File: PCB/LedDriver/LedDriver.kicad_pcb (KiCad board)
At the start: 2 copper layers, 101.6 x 101.6 mm, 157 parts, among them J101 LCD, J102 TweLite-R, J103 Conn_01x02_Male, J104 Conn_01x08_Male, J105 Conn_01x08_Male, J106 Conn_01x08_Male, J107 Conn_01x02_Male, J108 Barrel_Jack_Switch, J109 Conn_01x02_Male, J110 Conn_01x02_Male, SW101 SW_Push, SW102 SW_Push, SW103 SW_Push, SW104 SW_Push, SW105 SW_Push, SW106 SW_Push, SW107 SW_Push, U101 MW-R-WX, U201 NJW4617DL3-TE1, U202 NJW4617DL3-TE1, U203 NJW4617DL3-TE1, U204 NJW4617DL3-TE1, U205 NJW4617DL3-TE1, U206 NJW4617DL3-TE1, U207 NJW4617DL3-TE1, U208 74HC595, U301 NJW4617DL3-TE1, U302 NJW4617DL3-TE1, U303 NJW4617DL3-TE1, U304 NJW4617DL3-TE1, U305 NJW4617DL3-TE1, U306 NJW4617DL3-TE1, U307 NJW4617DL3-TE1, U308 74HC595, U401 NJW4617DL3-TE1, U402 NJW4617DL3-TE1, U403 NJW4617DL3-TE1, U404 NJW4617DL3-TE1, U405 NJW4617DL3-TE1, U406 NJW4617DL3-TE1, U407 NJW4617DL3-TE1, U408 74HC595

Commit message: 基板改良
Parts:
- added C106: 10u, Capacitor_SMD:C_0603_1608Metric, B.Cu at (240.0, 154.9)
- added C107: 10u, Capacitor_SMD:C_0603_1608Metric, B.Cu at (240.0, 142.2)
- added C108: 10u, Capacitor_SMD:C_0603_1608Metric, B.Cu at (219.7, 158.8)
- added C201: 0.1u, Capacitor_SMD:C_0603_1608Metric, B.Cu at (161.3, 49.5)
- added C202: 0.1u, Capacitor_SMD:C_0603_1608Metric, B.Cu at (161.3, 64.8)
- added C203: 0.1u, Capacitor_SMD:C_0603_1608Metric, B.Cu at (161.3, 80.0)
- added C204: 0.1u, Capacitor_SMD:C_0603_1608Metric, B.Cu at (161.3, 95.2)
- added C205: 0.1u, Capacitor_SMD:C_0603_1608Metric, B.Cu at (161.3, 110.5)
- added C206: 0.1u, Capacitor_SMD:C_0603_1608Metric, B.Cu at (161.3, 125.7)
- added C207: 0.1u, Capacitor_SMD:C_0603_1608Metric, B.Cu at (161.3, 141.0)
- added C208: 0.1u, Capacitor_SMD:C_0603_1608Metric, B.Cu at (143.5, 154.9)
- added C301: 0.1u, Capacitor_SMD:C_0603_1608Metric, B.Cu at (191.8, 49.5)
- added C302: 0.1u, Capacitor_SMD:C_0603_1608Metric, B.Cu at (191.8, 64.8)
- added C303: 0.1u, Capacitor_SMD:C_0603_1608Metric, B.Cu at (191.8, 80.0)
- added C304: 0.1u, Capacitor_SMD:C_0603_1608Metric, B.Cu at (191.8, 95.2)
- added C305: 0.1u, Capacitor_SMD:C_0603_1608Metric, B.Cu at (191.8, 110.5)
- added C306: 0.1u, Capacitor_SMD:C_0603_1608Metric, B.Cu at (191.8, 125.7)
- added C307: 0.1u, Capacitor_SMD:C_0603_1608Metric, B.Cu at (191.8, 141.0)
- added C308: 0.1u, Capacitor_SMD:C_0603_1608Metric, B.Cu at (174.0, 154.9)
- added C401: 0.1u, Capacitor_SMD:C_0603_1608Metric, B.Cu at (222.2, 49.5)
- added C402: 0.1u, Capacitor_SMD:C_0603_1608Metric, B.Cu at (222.2, 64.8)
- added C403: 0.1u, Capacitor_SMD:C_0603_1608Metric, B.Cu at (222.2, 80.0)
- added C404: 0.1u, Capacitor_SMD:C_0603_1608Metric, B.Cu at (222.2, 95.2)
- added C405: 0.1u, Capacitor_SMD:C_0603_1608Metric, B.Cu at (222.2, 110.5)
- added C406: 0.1u, Capacitor_SMD:C_0603_1608Metric, B.Cu at (222.2, 125.7)
- added C407: 0.1u, Capacitor_SMD:C_0603_1608Metric, B.Cu at (222.2, 141.0)
- added C408: 0.1u, Capacitor_SMD:C_0603_1608Metric, B.Cu at (204.5, 154.9)
- added H105: MountingHole, MountingHole:MountingHole_6.4mm_M6, F.Cu at (128.3, 52.1)
- added J111: Conn_01x02_Male, Connector_JST:JST_XH_B2B-XH-A_1x02_P2.50mm_Vertical, B.Cu at (214.6, 158.8)
- added U102: LM1117-3.3, Package_TO_SOT_SMD:SOT-223-3_TabPin2, B.Cu at (240.0, 148.6)
- C102: value 0.1u -> 10u; footprint Capacitor_SMD:C_1206_3216Metric -> Capacitor_SMD:C_0603_1608Metric
- C103: value 10u -> 0.1u; footprint Capacitor_THT:CP_Radial_D10.0mm_P5.00mm -> Capacitor_SMD:C_0603_1608Metric
- C104: footprint Capacitor_SMD:C_0603_1608Metric -> Capacitor_SMD:C_1206_3216Metric
- C105: value 47u -> 10u; footprint Capacitor_SMD:C_0603_1608Metric -> Capacitor_THT:CP_Radial_D10.0mm_P5.00mm; moved to F.Cu
- J102: value TweLite-R -> Conn_01x07_Female; footprint Connector_PinSocket_2.54mm:PinSocket_1x06_P2.54mm_Vertical -> Connector_PinSocket_2.54mm:PinSocket_1x07_P2.54mm_Vertical
- J104: value Conn_01x08_Male -> Conn_01x02_Male; footprint Connector_JST:JST_VH_B8P-VH_1x08_P3.96mm_Vertical -> Connector_JST:JST_VH_B2P-VH_1x02_P3.96mm_Vertical
- J105, J106: value Conn_01x08_Male -> Conn_01x02_Male; footprint Connector_JST:JST_VH_B8P-VH_1x08_P3.96mm_Vertical -> Connector_PinHeader_2.54mm:PinHeader_1x02_P2.54mm_Vertical
- J107: value Conn_01x02_Male -> DC+5V; footprint Connector_JST:JST_VH_B2P-VH_1x02_P3.96mm_Vertical -> Connector_BarrelJack:BarrelJack_CUI_PJ-102AH_Horizontal
- J108: value Barrel_Jack_Switch -> Conn_01x08_Male; footprint Connector_BarrelJack:BarrelJack_CUI_PJ-102AH_Horizontal -> Connector_JST:JST_VH_B8P-VH_1x08_P3.96mm_Vertical
- J109, J110: value Conn_01x02_Male -> Conn_01x08_Male; footprint Connector_PinHeader_2.54mm:PinHeader_1x02_P2.54mm_Vertical -> Connector_JST:JST_VH_B8P-VH_1x08_P3.96mm_Vertical
- R201, R204, R207, R210, R213, R216, R219, R301, R304, R307, R310, R313, R316, R319, R401, R404, R407, R410, R413, R416, R419: value 680 -> 1.2k
- R202, R205, R208, R211, R214, R217, R220, R302, R305, R308, R311, R314, R317, R320, R402, R405, R408, R411, R414, R417, R420: value 0.33 -> 0.20; footprint Resistor_THT:R_Axial_DIN0207_L6.3mm_D2.5mm_P7.62mm_Horizontal -> Resistor_THT:R_Axial_DIN0207_L6.3mm_D2.5mm_P10.16mm_Horizontal; moved to F.Cu
- R203, R206, R209, R212, R215, R218, R221, R303, R306, R309, R312, R315, R318, R321, R403, R406, R409, R412, R415, R418, R421: value 0.33 -> 0.47; footprint Resistor_THT:R_Axial_DIN0207_L6.3mm_D2.5mm_P7.62mm_Horizontal -> Resistor_THT:R_Axial_DIN0207_L6.3mm_D2.5mm_P10.16mm_Horizontal; moved to F.Cu
- R222, R223, R224, R225, R226, R227, R228, R322, R323, R324, R325, R326, R327, R328, R422, R423, R424, R425, R426, R427, R428: value 1k -> 1.2k
- U201, U202, U203, U204, U205, U206, U207: moved to B.Cu
- moved J110 152.3 mm to (238.8, 47.6), turned to -90 degrees
- moved J107 131.0 mm to (232.9, 155.1)
- moved R322 126.3 mm to (188.0, 52.1), turned to 90 degrees
- moved J109 123.1 mm to (208.3, 47.6), turned to -90 degrees
- moved R328 116.8 mm to (188.0, 143.5), turned to 90 degrees
- moved R302 114.4 mm to (198.1, 55.9), turned to 180 degrees
- moved R305 114.4 mm to (198.1, 71.1), turned to 180 degrees
- moved R308 114.3 mm to (198.1, 86.4), turned to 180 degrees
- moved R311 114.3 mm to (198.1, 101.6), turned to 180 degrees
- moved R320 114.3 mm to (198.1, 147.3), turned to 180 degrees
- moved R314 114.3 mm to (198.1, 116.8), turned to 180 degrees
- moved R317 114.3 mm to (198.1, 132.1), turned to 180 degrees
- moved R422 114.1 mm to (218.4, 52.1), turned to 90 degrees
- moved J108 113.4 mm to (177.8, 47.6), turned to -90 degrees
- moved D301 108.7 mm to (195.6, 52.1)
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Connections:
- C102 pad 1: VDD -> GND
- C102 pad 2: GND -> +3.3V
- C103 pad 1: VDD -> +3.3V
- C104 pad 1: +3.3V -> VDD
- C105 pad 1: +3.3V -> VDD
- J104 pad 2: /digitDriver_one/A -> GND
- J105 pad 1: VDD -> /add_01
- J105 pad 2: /digitDriver_ten/A -> GND
- J106 pad 1: VDD -> /add_02
- J106 pad 2: /digitDriver_hun/A -> GND
- J107 pad 1: VDD -> Net-(C106-Pad1)
- J108 pad 1: +3.3V -> VDD
- J108 pad 2: GND -> /digitDriver_one/A
- J108 pad 3: unconnected-(J108-Pad3) -> /digitDriver_one/B
- J109 pad 1: /add_01 -> VDD
- J109 pad 2: GND -> /digitDriver_ten/A
- J110 pad 1: /add_02 -> VDD
- J110 pad 2: GND -> /digitDriver_hun/A
- R203 pad 1: Net-(R202-Pad1) -> Net-(R202-Pad2)
- R206 pad 1: Net-(R205-Pad1) -> Net-(R205-Pad2)
- R209 pad 1: Net-(R208-Pad1) -> Net-(R208-Pad2)
- R212 pad 1: Net-(R211-Pad1) -> Net-(R211-Pad2)
- R215 pad 1: Net-(R214-Pad1) -> Net-(R214-Pad2)
- R218 pad 1: Net-(R217-Pad1) -> Net-(R217-Pad2)
- R221 pad 1: Net-(R220-Pad1) -> Net-(R220-Pad2)
- R222 pad 1: /digitDriver_one/QG -> /digitDriver_one/QA
- R223 pad 1: /digitDriver_one/QF -> /digitDriver_one/QB
- R224 pad 1: /digitDriver_one/QE -> /digitDriver_one/QC
- R226 pad 1: /digitDriver_one/QC -> /digitDriver_one/QE
- R227 pad 1: /digitDriver_one/QB -> /digitDriver_one/QF
- R228 pad 1: /digitDriver_one/QA -> /digitDriver_one/QG
- R303 pad 1: Net-(R302-Pad1) -> Net-(R302-Pad2)
- R306 pad 1: Net-(R305-Pad1) -> Net-(R305-Pad2)
- R309 pad 1: Net-(R308-Pad1) -> Net-(R308-Pad2)
- R312 pad 1: Net-(R311-Pad1) -> Net-(R311-Pad2)
- R315 pad 1: Net-(R314-Pad1) -> Net-(R314-Pad2)
- R318 pad 1: Net-(R317-Pad1) -> Net-(R317-Pad2)
- R321 pad 1: Net-(R320-Pad1) -> Net-(R320-Pad2)
- R322 pad 1: /digitDriver_ten/QG -> /digitDriver_ten/QA
- R323 pad 1: /digitDriver_ten/QF -> /digitDriver_ten/QB
- R324 pad 1: /digitDriver_ten/QE -> /digitDriver_ten/QC
- R326 pad 1: /digitDriver_ten/QC -> /digitDriver_ten/QE
- R327 pad 1: /digitDriver_ten/QB -> /digitDriver_ten/QF
- R328 pad 1: /digitDriver_ten/QA -> /digitDriver_ten/QG
- R403 pad 1: Net-(R402-Pad1) -> Net-(R402-Pad2)
- R406 pad 1: Net-(R405-Pad1) -> Net-(R405-Pad2)
- R409 pad 1: Net-(R408-Pad1) -> Net-(R408-Pad2)
- R412 pad 1: Net-(R411-Pad1) -> Net-(R411-Pad2)
- R415 pad 1: Net-(R414-Pad1) -> Net-(R414-Pad2)
- R418 pad 1: Net-(R417-Pad1) -> Net-(R417-Pad2)
- R421 pad 1: Net-(R420-Pad1) -> Net-(R420-Pad2)
- R422 pad 1: /digitDriver_hun/QG -> /digitDriver_hun/QA
- R423 pad 1: /digitDriver_hun/QF -> /digitDriver_hun/QB
- R424 pad 1: /digitDriver_hun/QE -> /digitDriver_hun/QC
- R426 pad 1: /digitDriver_hun/QC -> /digitDriver_hun/QE
- R427 pad 1: /digitDriver_hun/QB -> /digitDriver_hun/QF
- R428 pad 1: /digitDriver_hun/QA -> /digitDriver_hun/QG
- U201 pad 4: Net-(R202-Pad2) -> Net-(R202-Pad1)
- U202 pad 4: Net-(R205-Pad2) -> Net-(R205-Pad1)
- U203 pad 4: Net-(R208-Pad2) -> Net-(R208-Pad1)
- U204 pad 4: Net-(R211-Pad2) -> Net-(R211-Pad1)
- U205 pad 4: Net-(R214-Pad2) -> Net-(R214-Pad1)
- U206 pad 4: Net-(R217-Pad2) -> Net-(R217-Pad1)
- U207 pad 4: Net-(R220-Pad2) -> Net-(R220-Pad1)
- U301 pad 4: Net-(R302-Pad2) -> Net-(R302-Pad1)
- U302 pad 4: Net-(R305-Pad2) -> Net-(R305-Pad1)
- U303 pad 4: Net-(R308-Pad2) -> Net-(R308-Pad1)
- U304 pad 4: Net-(R311-Pad2) -> Net-(R311-Pad1)
- U305 pad 4: Net-(R314-Pad2) -> Net-(R314-Pad1)
- U306 pad 4: Net-(R317-Pad2) -> Net-(R317-Pad1)
- U307 pad 4: Net-(R320-Pad2) -> Net-(R320-Pad1)
- U401 pad 4: Net-(R402-Pad2) -> Net-(R402-Pad1)
- U402 pad 4: Net-(R405-Pad2) -> Net-(R405-Pad1)
- U403 pad 4: Net-(R408-Pad2) -> Net-(R408-Pad1)
- U404 pad 4: Net-(R411-Pad2) -> Net-(R411-Pad1)
- U405 pad 4: Net-(R414-Pad2) -> Net-(R414-Pad1)
- U406 pad 4: Net-(R417-Pad2) -> Net-(R417-Pad1)
- U407 pad 4: Net-(R420-Pad2) -> Net-(R420-Pad1)
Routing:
- net +3.3V: track 510.8 -> 795.7 mm, vias 10 -> 1
- net /digitDriver_ten/QG: track 78.4 -> 12.4 mm, vias 1 -> 2
- net /digitDriver_ten/F: track 118.3 -> 62.6 mm
- net /digitDriver_hun/QG: track 70.3 -> 15.6 mm, vias 2 -> 1
- net /digitDriver_ten/QF: track 66.0 -> 24.6 mm, vias 2 -> 1
- net /digitDriver_ten/QC: track 33.6 -> 71.9 mm, vias 1 -> 2
- net /SCK: track 89.6 -> 127.2 mm, vias 3 -> 2
- net /digitDriver_ten/QB: track 52.3 -> 88.5 mm, vias 1 -> 2
- net /digitDriver_hun/QC: track 36.4 -> 72.5 mm
- net /RESET: track 97.1 -> 132.6 mm
- net /_G: track 81.1 -> 115.1 mm, vias 3 -> 0
- net Net-(C106-Pad1): track 0.00 -> 33.5 mm
- net /SI: track 36.9 -> 68.7 mm
- net /_SCLR: track 78.2 -> 109.8 mm
- net /SCL: track 31.3 -> 61.8 mm
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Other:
- board size 101.6 x 101.6 mm -> 125.7 x 125.7 mm
- board text removed: "+"
- board text removed: "+ -"
- board text removed: "-"
- board text removed: "1"
- board text removed: "1'"
- board text removed: "10'"
- board text removed: "100'"
- board text removed: "ADDR_H"
- board text removed: "ADDR_L"
- board text removed: "Ah"
- board text removed: "Ao"
- board text removed: "At"
- board text removed: "Bh"
- board text removed: "Bo"
- board text removed: "Bt"
- board text removed: "Ch"
- board text removed: "Co"
- board text removed: "Ct"
- board text removed: "DC3.3V"
- board text removed: "DC36V"
- board text removed: "Dh"
- board text removed: "Do"
- board text removed: "Dt"
- board text removed: "Eh"
- board text removed: "Eo"
- board text removed: "Et"
- board text removed: "Fh"
- board text removed: "Fo"
- board text removed: "Ft"
- board text removed: "Gh"
- board text removed: "Go"
- board text removed: "Gt"
- board text removed: "Reset"

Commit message: 回路修正
三端子レギュレータ追加
GNDパターン修正
currentパターン同士のクリアランスを確保
ファン端子追加
温度センサ追加
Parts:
- added C109: 0.1u, Capacitor_SMD:C_0603_1608Metric, B.Cu at (201.3, 114.9)
- added U103: LM35-LP, Package_TO_SOT_THT:TO-92_Inline_Horizontal1, F.Cu at (203.2, 116.2)
- SW101, SW102, SW103, SW104, SW105, SW106, SW107: footprint Button_Switch_SMD:SW_SPST_B3S-1000 -> Library:SW_SPST_B3S-1000
- moved C107 113.1 mm to (127.0, 146.1)
- moved U102 113.1 mm to (127.0, 152.4)
- moved C106 111.8 mm to (128.3, 158.1)
- moved J107 99.1 mm to (134.0, 149.2)
- moved J111 21.6 mm to (236.2, 159.4)
- moved C108 15.6 mm to (234.9, 155.6), turned to 180 degrees
- moved C102 9.40 mm to (141.7, 119.6)
- moved C101 8.77 mm to (139.8, 119.6)
- moved U101 7.56 mm to (130.9, 119.6)
- moved R101 4.02 mm to (147.3, 152.4)
- moved SW101 4.02 mm to (147.3, 147.3)
- moved SW103 4.02 mm to (147.3, 139.7)
- moved SW105 4.02 mm to (137.2, 139.7)
- moved SW107 4.02 mm to (127.0, 139.7)
- moved SW102 4.02 mm to (147.3, 132.1)
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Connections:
- U101 pad 23: unconnected-(U101-Pad23) -> /ADC1
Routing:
- net VDD: track 37.6 -> 228.0 mm
- net Net-(C106-Pad1): track 33.5 -> 136.9 mm
- net /ADC1: track 0.00 -> 87.0 mm, vias 0 -> 1
- net +3.3V: track 795.7 -> 828.2 mm, vias 1 -> 3
- net /SI: track 68.7 -> 40.5 mm, vias 2 -> 0
- net /PlusHun: track 17.3 -> 3.77 mm
- net /TX: track 39.3 -> 52.6 mm
- net /SCK: track 127.2 -> 114.3 mm, vias 2 -> 3
- net /_SCLR: track 109.8 -> 122.6 mm, vias 3 -> 2
- net /MinusHun: track 24.6 -> 13.1 mm
- net /RCK: track 111.4 -> 120.6 mm, vias 2 -> 0
- net /PRG: track 30.7 -> 24.7 mm
- net Net-(R402-Pad1): track 10.4 -> 5.80 mm, vias 1 -> 0
- net Net-(R202-Pad1): track 10.5 -> 5.97 mm, vias 1 -> 0
- net /PlusOne: track 21.1 -> 17.1 mm
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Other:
- board text added: "+"
- board text added: "-"
- board text added: "1'"
- board text added: "1'A"
- board text added: "1'B"
- board text added: "1'C"
- board text added: "1'D"
- board text added: "1'E"
- board text added: "1'F"
- board text added: "1'G"
- board text added: "10'"
- board text added: "10'A"
- board text added: "10'B"
- board text added: "10'C"
- board text added: "10'D"
- board text added: "10'E"
- board text added: "10'F"
- board text added: "10'G"
- board text added: "100'"
- board text added: "100'A"
- board text added: "100'B"
- board text added: "100'C"
- board text added: "100'D"
- board text added: "100'E"
- board text added: "100'F"
- board text added: "100'G"
- board text added: "Addr1"
- board text added: "Addr2"
- board text added: "DC +5V"
- board text added: "DC 36V"
- board text added: "EXT"
- board text added: "Fan +5V"
- board text added: "LCD"
- board text added: "T-sens"
- board text added: "TWE-R"

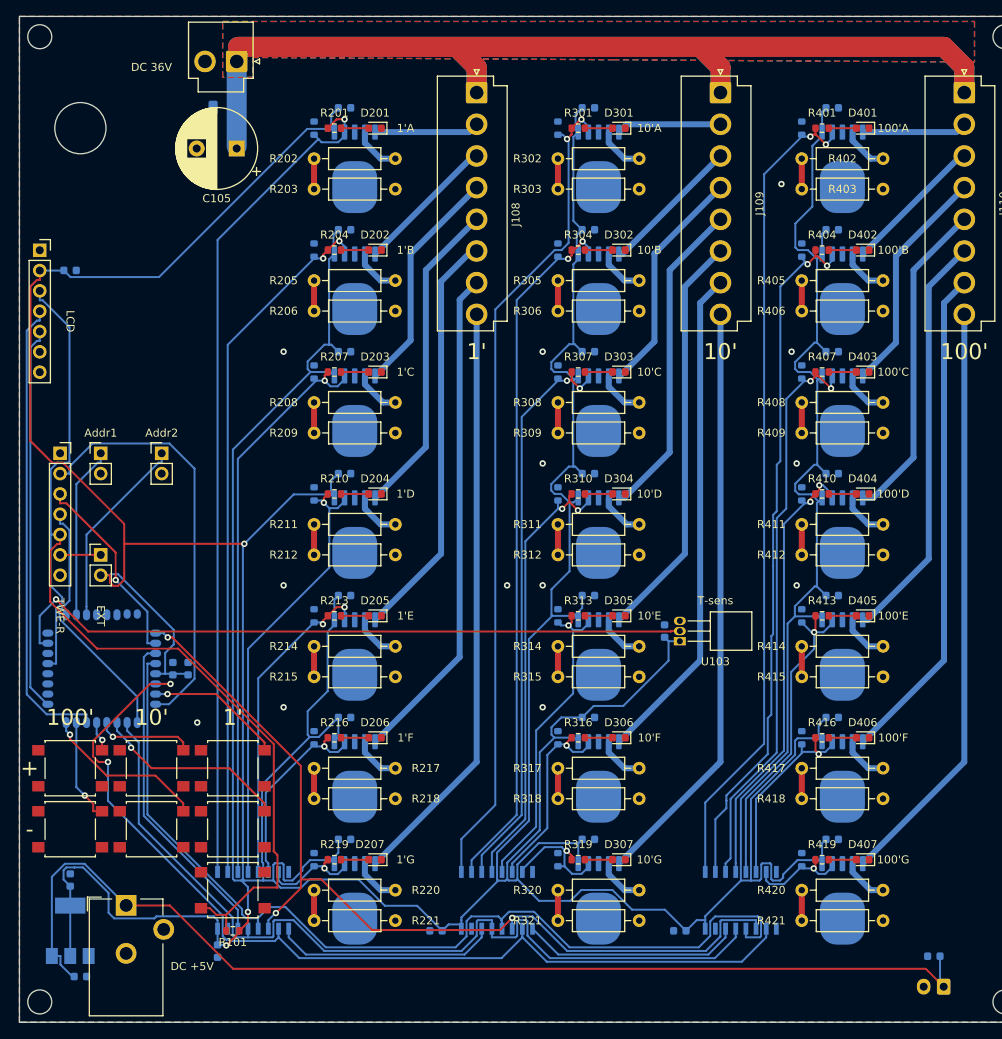
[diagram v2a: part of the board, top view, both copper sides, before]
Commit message: パターン修正
LEDドライバのパスコンを最短で配線
LEDドライバのタブをGNDに配線
平行な信号パターン同士の距離を開け、GNDパターンを間に追加
直角なパターンを修正
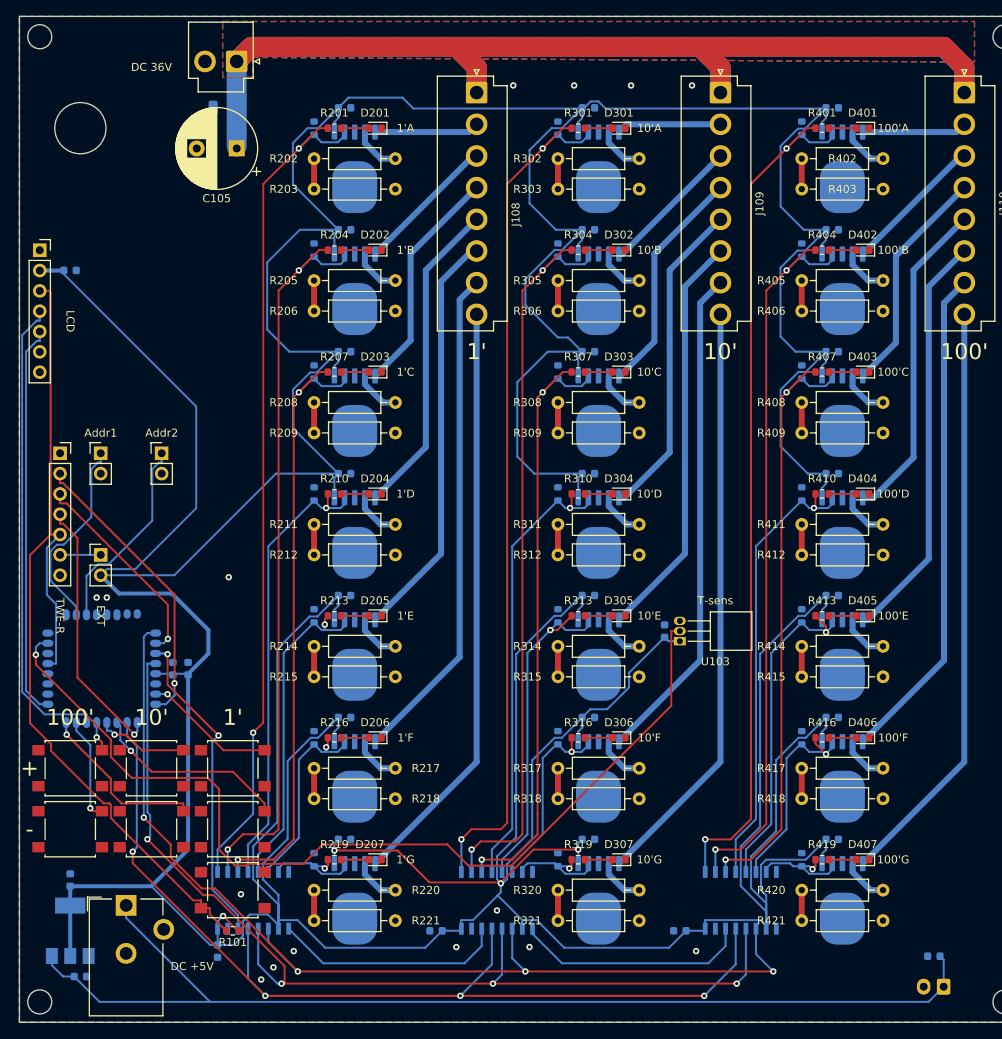
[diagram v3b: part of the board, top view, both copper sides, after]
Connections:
- U101 pad 6: /_SCLR -> unconnected-(U101-Pad6)
- U201 pad 6: unconnected-(U201-Pad6) -> GND
- U202 pad 6: unconnected-(U202-Pad6) -> GND
- U203 pad 6: unconnected-(U203-Pad6) -> GND
- U204 pad 6: unconnected-(U204-Pad6) -> GND
- U205 pad 6: unconnected-(U205-Pad6) -> GND
- U206 pad 6: unconnected-(U206-Pad6) -> GND
- U207 pad 6: unconnected-(U207-Pad6) -> GND
- U208 pad 10: /_SCLR -> +3.3V
- U301 pad 6: unconnected-(U301-Pad6) -> GND
- U302 pad 6: unconnected-(U302-Pad6) -> GND
- U303 pad 6: unconnected-(U303-Pad6) -> GND
- U304 pad 6: unconnected-(U304-Pad6) -> GND
- U305 pad 6: unconnected-(U305-Pad6) -> GND
- U306 pad 6: unconnected-(U306-Pad6) -> GND
- U307 pad 6: unconnected-(U307-Pad6) -> GND
- U308 pad 10: /_SCLR -> +3.3V
- U401 pad 6: unconnected-(U401-Pad6) -> GND
- U402 pad 6: unconnected-(U402-Pad6) -> GND
- U403 pad 6: unconnected-(U403-Pad6) -> GND
- U404 pad 6: unconnected-(U404-Pad6) -> GND
- U405 pad 6: unconnected-(U405-Pad6) -> GND
- U406 pad 6: unconnected-(U406-Pad6) -> GND
- U407 pad 6: unconnected-(U407-Pad6) -> GND
- U408 pad 10: /_SCLR -> +3.3V
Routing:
- net /_SCLR: track 122.6 -> 0.00 mm, vias 2 -> 0
- net +3.3V: track 828.2 -> 903.5 mm, vias 3 -> 4
- net /ADC1: track 87.0 -> 120.3 mm
- net /SCK: track 114.3 -> 131.0 mm, vias 3 -> 4
- net /TX: track 52.6 -> 36.7 mm, vias 0 -> 1
- net /RESET: track 129.1 -> 113.6 mm
- net /_G: track 111.6 -> 125.9 mm, vias 0 -> 4
- net /RCK: track 120.6 -> 129.1 mm, vias 0 -> 4
- net /digitDriver_one/QC: track 71.7 -> 78.2 mm, vias 1 -> 2
- net /digitDriver_ten/QB: track 87.6 -> 93.9 mm
- net /digitDriver_one/QB: track 87.6 -> 93.6 mm
- net /digitDriver_ten/QC: track 71.8 -> 77.6 mm
- net /digitDriver_hun/QA: track 103.5 -> 108.9 mm
- net /digitDriver_hun/QB: track 88.0 -> 93.2 mm
- net /digitDriver_hun/QC: track 72.3 -> 77.2 mm
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
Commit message: パターン修正
シフトレジスタ信号線と平行な3.3Vラインを移動
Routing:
- net +3.3V: track 903.5 -> 788.5 mm, vias 4 -> 13
- net /ADC1: track 120.3 -> 127.8 mm
- net /digitDriver_hun/QF: track 26.5 -> 28.7 mm
- net /digitDriver_hun/QE: track 42.2 -> 43.7 mm

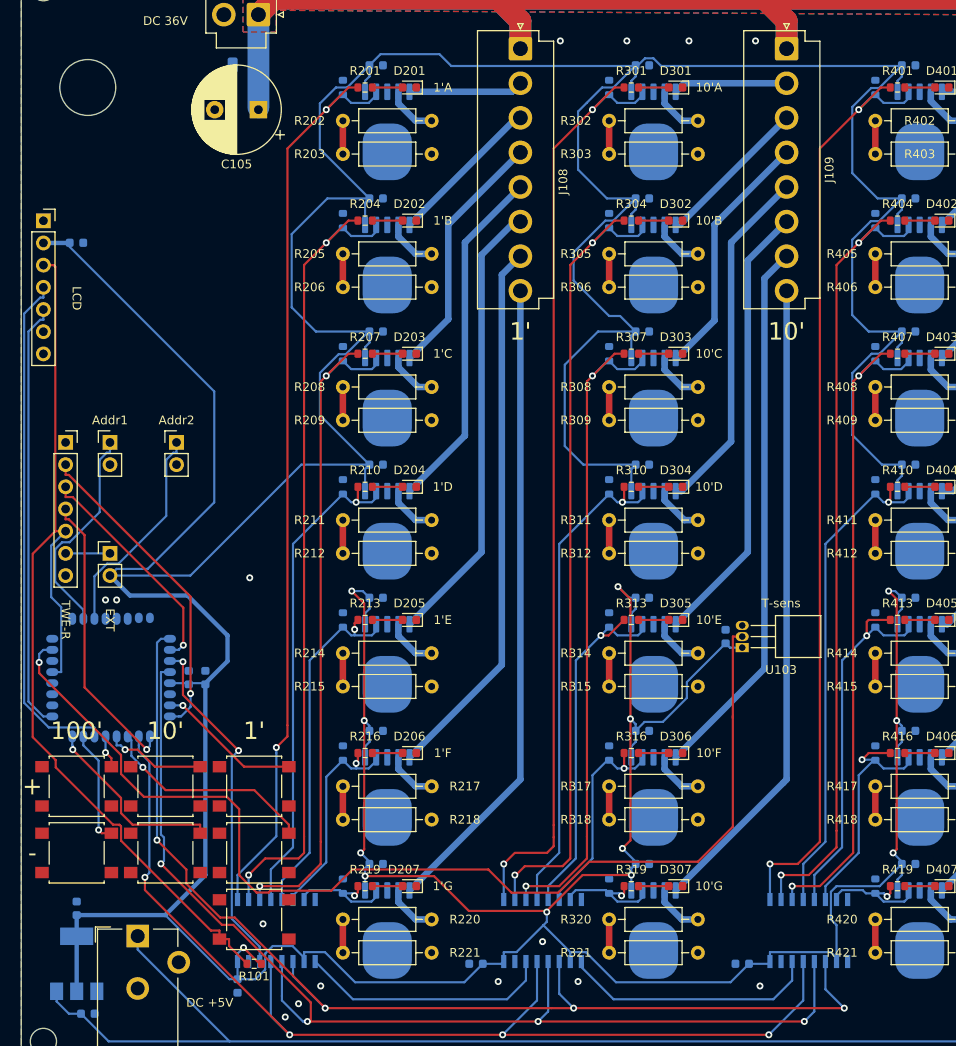
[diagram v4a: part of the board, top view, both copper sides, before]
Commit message: パターン修正
3.3V系を0.4mm幅に変更
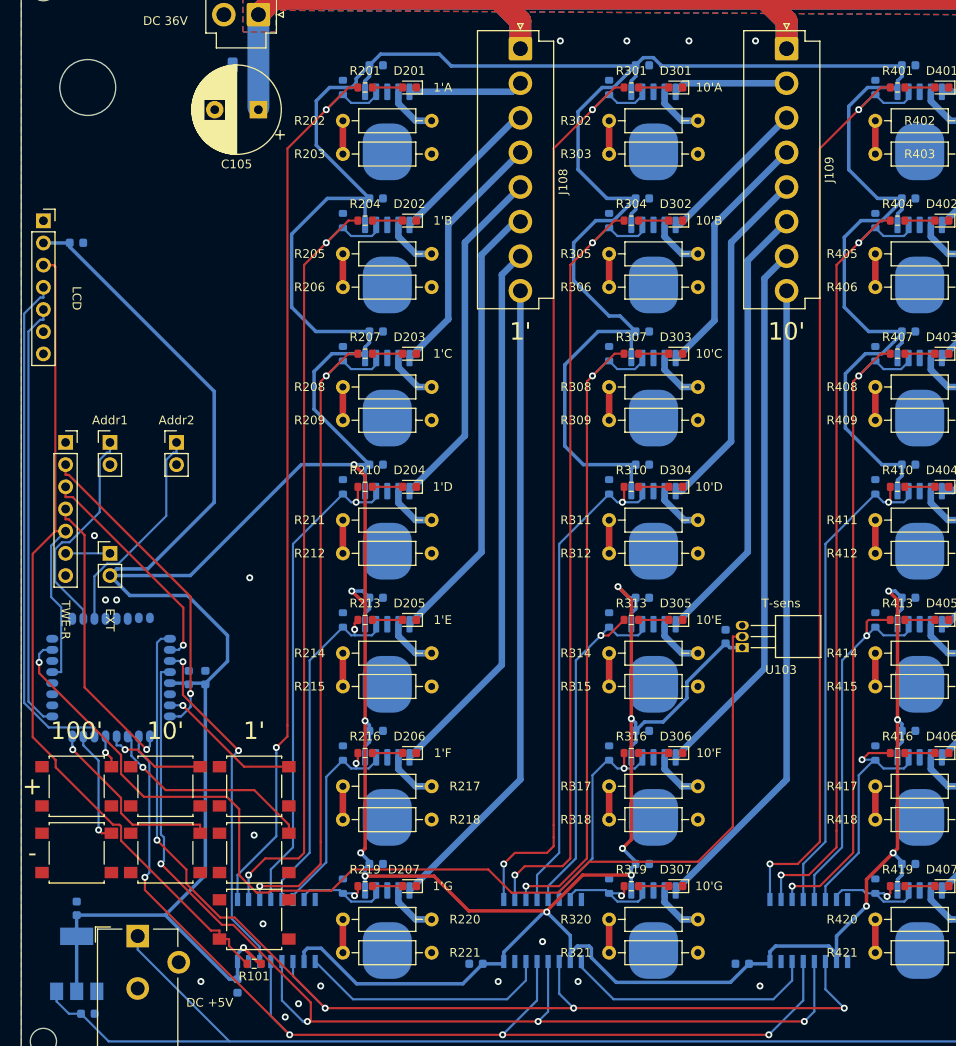
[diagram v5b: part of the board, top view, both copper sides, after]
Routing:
- net +3.3V: track 788.5 -> 799.9 mm, vias 13 -> 15
- net GND: vias 15 -> 18
